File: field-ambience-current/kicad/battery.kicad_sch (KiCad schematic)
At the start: 22 parts, among them J9 JST PH 2.0 2-pin (LiPo Batter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, U7 MCP73831T-2ACI/OT (LiPo Charg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, U8 TPS61089RNR (Boost LiPo→5V, 2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

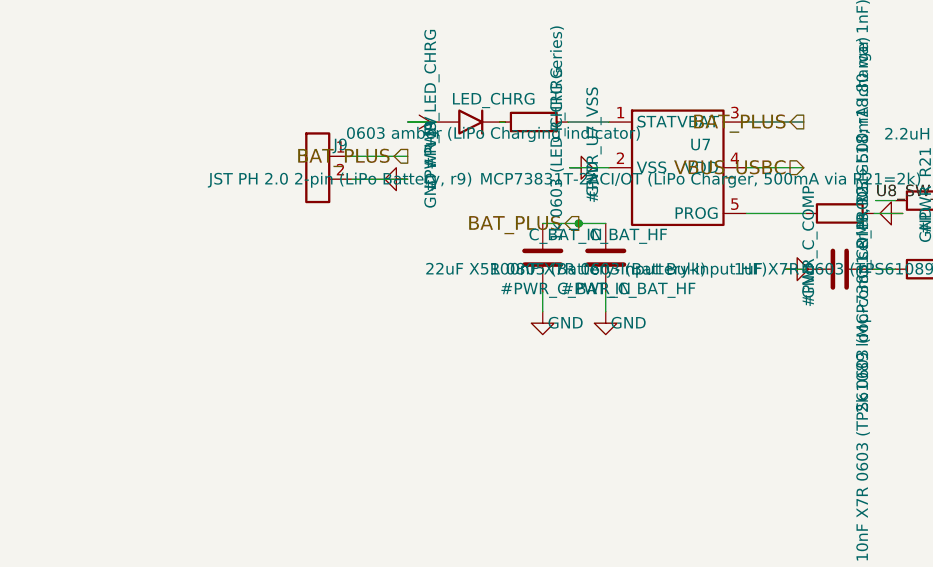
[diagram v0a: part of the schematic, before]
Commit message: fix(pcb): datasheet verification of all remaining parts — encoder + jack pad maps were dead/wrong (r18.82) (#94)
User asked to verify all other components against datasheets. Every
remaining IC and every symbol-pin<->footprint-pad pairing was checked
against the official documents (Microchip DS20001952 + DS20001984, NXP
PCA9685 Rev 4, ST USBLC6-2 + DS12110 Fig 5, Abracon via LCSC, SHOU HAN
PJ-320D, HX B3F-4055, KiCad footprint sources).

Critical pad-mapping bugs (KiCad matches pin number to pad name as a
STRING):

1. All 4 rotary encoders were completely unconnected: the official KiCad
   footprint RotaryEncoder_Alps_EC11E-Switch_Vertical_H20mm uses NAMED
   pads A/B/C/S1/S2, the custom symbol used numeric pins 1-5 - not a
   single encoder pin would have joined a pad in the netlist. Symbol pin
   numbers renamed to the pad names (footprint geometry verified from
   the KiCad GitLab source: A(0,0), C(0,2.5) = middle common, B(0,5) =
   ALPS A-C-B terminal order).

2. PJ-320D jacks (J8 line-out, J10 MIDI): pad map was wrong. The SHOU HAN
   drawing (PCB layout + schematic) assigns pad 1=A=sleeve, 2=D=ring,
   3=C=tip-switch(detect), 4=B=tip. The symbol mapped T=1/R=2/S=3/DET=4,
   which put LEFT AUDIO on the grounded sleeve barrel, GND on the detect
   contact and JACK_DETECT on the tip. Corrected to T=4/R=2/S=1/DET=3.
   Vendored footprint geometry matches the drawing exactly (3.0/4.0mm
   pad pitch, 1.0mm locators at 7.0mm) - closes TODO B0b.

3. Consequence of the true detect topology (detect rests on the TIP when
   unplugged, i.e. on the DAC L output at +-3Vpk): added R_DET_J8 10k
   (limits MCP input-clamp current to <300uA - unprotected it would have
   clamped negative half-waves through 22R at >100mA, distorting the
   speaker feed) and C_DET_J8 1uF (filters audio AC off GPA6, fc ~16Hz).
   Levels: unplugged ~0.3V LOW, plugged 3.3V HIGH.

Datasheet-required gaps:

4. MCP73831 was missing the 4.7uF VDD input capacitor from the DS typical
   application - the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
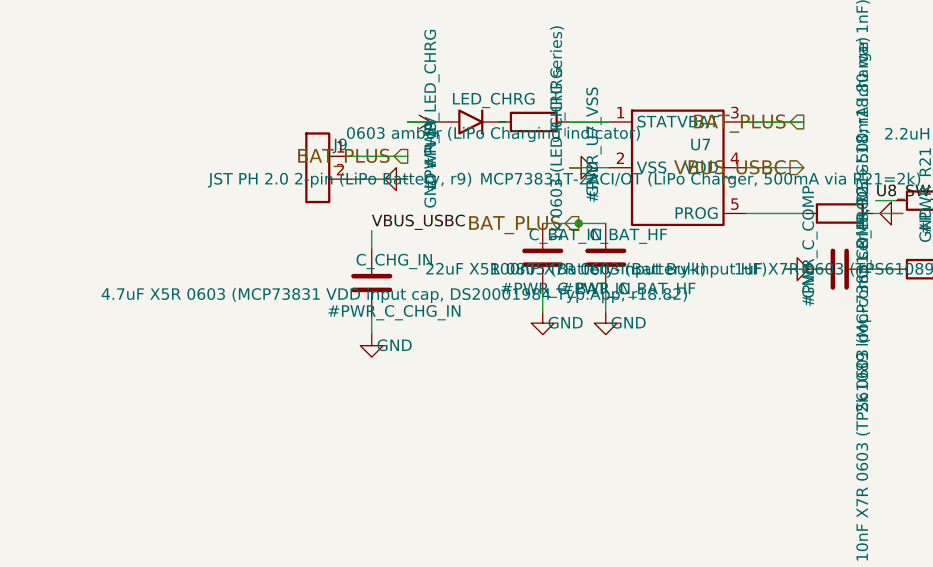
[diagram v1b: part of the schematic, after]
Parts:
- added C_CHG_IN: 4.7uF X5R 0603 (MCP73831 VDD input cap, DS2000198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, Capacitor_SMD:C_0603_1608Metric, symbol Device:C
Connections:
- net GND: now also C_CHG_IN.2
- net VBUS_USBC: now also C_CHG_IN.1
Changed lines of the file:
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@@
       (project "field_ambience"
         (path "/f6a664dc-7032-4108-a10b-e4076008e6bd" (reference "#PWR_LED_CHRG") (unit 1)))))
+  (symbol (lib_id "Device:C") (at 56 92.81 0) (unit 1)
+    (in_bom yes) (on_board yes) (dnp no)
+      (property "Reference" "C_CHG_IN" (at 58.54 90.27 0)
+        (effects (font (size 1.27 1.27))))
+      (property "Value" "4.7uF X5R 0603 (MCP73831 VDD input cap, DS20001984 Typ.App; r18.82)" (at 58.54 94.08 0)
+        (effects (font (size 1.27 1.27))))
+      (property "Footprint" "Capacitor_SMD:C_0603_1608Metric" (at 56 92.81 0)
+        (effects (font (size 1.27 1.27)) hide))
+      (property "Datasheet" "~" (at 56 92.81 0)
+        (effects (font (size 1.27 1.27)) hide))
+      (property "MPN" "GRM188R61A475KE15D" (at 58.54 96.62 0)
+        (effects (font (size 1.27 1.27)) hide))
+      (property "LCSC" "C46653" (at 58.54 97.89 0)
+        (effects (font (size 1.27 1.27)) hide))
+    (instances
+      (project "field_ambience"
+        (path "/f6a664dc-7032-4108-a10b-e4076008e6bd" (reference "C_CHG_IN") (unit 1)))))
+  (symbol (lib_id "Power:GND") (at 56 98.5 0) (unit 1)
+    (in_bom yes) (on_board yes) (dnp no)
+      (property "Reference" "#PWR_C_CHG_IN" (at 58.54 95.96 0)
+        (effects (font (size 1.27 1.27))))
+      (property "Value" "GND" (at 58.54 99.77 0)
+        (effects (font (size 1.27 1.27))))
+      (property "Footprint" "" (at 56 98.5 0)
+        (effects (font (size 1.27 1.27)) hide))
+      (property "Datasheet" "~" (at 56 98.5 0)
+        (effects (font (size 1.27 1.27)) hide))
+    (instances
+      (project "field_ambience"
+        (path "/f6a664dc-7032-4108-a10b-e4076008e6bd" (reference "#PWR_C_CHG_IN") (unit 1)))))
   (symbol (lib_id "Device:R") (at 108.0 85.08 90) (unit 1)
     (in_bom yes) (on_board yes) (dnp no)
@@
     (stroke (width 0) (type default))
 )
+  (wire (pts (xy 56 87) (xy 56 89))
+    (stroke (width 0) (type default))
+)
+  (wire (pts (xy 56 96.62) (xy 56 98.5))
+    (stroke (width 0) (type default))
+)
   (wire (pts (xy 97.62 74.92) (xy 104.0 74.92))
     (stroke (width 0) (type default))
@@
   (junction (at 140 83.65) (diameter 0) (color 0 0 0 0)
 )
+  (label "VBUS_USBC" (at 56 87 0) (fields_autoplaced)
+    (effects (font (size 1.27 1.27)) (justify left bottom))
+)
   (label "U8_SW_NODE" (at 141 83.65 0) (fields_autoplaced)

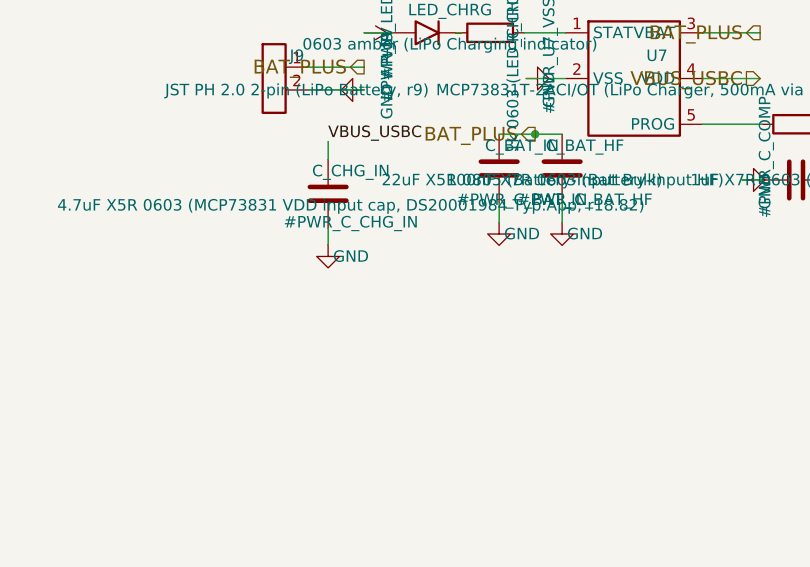
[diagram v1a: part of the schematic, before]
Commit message: fix(pcb): both PCA9685 /OE pull-ups had no driver — LEDs would never light; +mounting holes +test points +cost estimate (r18.84)
User asked whether any must-have components are missing, and for a fresh
JLC cost estimate.

CRITICAL find: both PCA9685 output-enable pins (R_OE on U6, R_OE2 on U10)
were pulled HIGH to +3V3 with a comment claiming firmware drives /OE low
after PWM init — but no net connected /OE to any MCU/MCP pin, so nothing
could ever drive it. /OE would sit HIGH forever: all 15 status LEDs, the
LCD backlight AND the 8 VU LEDs permanently disabled (backlight off = the
screen is unreadable). Fixed to pull-DOWN (outputs always enabled).
Boot-dark is still guaranteed by the chip itself: NXP datasheet Table 7,
LEDn_OFF_H[4] 'full OFF' defaults to 1 on every channel, verified against
the PDF — the part powers up with every channel in FULL_OFF regardless of
/OE. Firmware pca_init comments updated to match (nothing to sequence).

Added missing must-haves:
- 4x M2.5 mounting holes H1-H4 (plated, GND) — defined in the mechanical
  spec section 6 all along ((12,6)/(240,6)/(12,96)/(240,96)) but never in
  the schematic. DNP symbols with footprint MountingHole_2.7mm_M2.5_Pad
  (FP note: KiCad's 5.4mm pad vs the spec's 6mm — a layout call for Aron).
- 7 test points (AI_READY schematic standard requires TP_*): TP_5V,
  TP_3V3, TP_5VSW, TP_VBUS, TP_GND1/2 on power_tree + TP_BAT on battery,
  all DNP TestPoint_Pad_D1.5mm.
Both are fit-free, so jlc_bom.csv is unchanged at 58 parts / 210
placements (the exporter correctly skips the 11 DNP items).

Completeness sweep otherwise clean: USB protection (fuse+TVS+ESD+CC),
charge/power path incl. on/off (since r18.81), NRST/BOOT0, VCAP, HSE +
loads, I2C pull-ups, status LED, backlight driver, SWD, jack clamp
(r18.82). Deliberately NOT on the PCB (not defects): battery protection
PCM (must live in the LiPo pouch — buy note added), fiducials (JLC adds
them at panelization), MIDI-IN (OUT only per ADR-0004).

Cost estimate rebuilt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
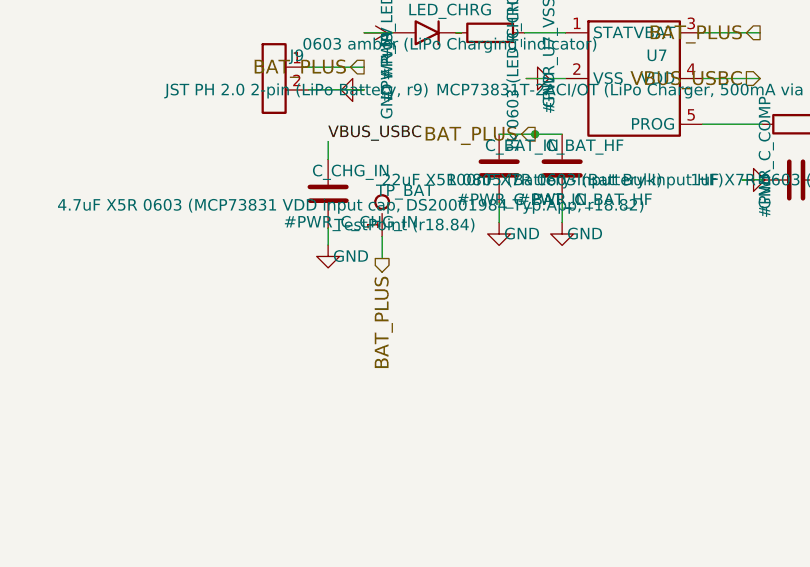
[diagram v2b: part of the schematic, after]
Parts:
- added TP_BAT: TestPoint (r18.84), TestPoint:TestPoint_Pad_D1.5mm, symbol Connector:TestPoint
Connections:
- net BAT_PLUS: now also TP_BAT.1
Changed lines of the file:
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@@
       (project "field_ambience"
         (path "/f6a664dc-7032-4108-a10b-e4076008e6bd" (reference "#PWR_C_BAT_IN") (unit 1)))))
+  (symbol (lib_id "Connector:TestPoint") (at 62 95 0) (unit 1)
+    (in_bom yes) (on_board yes) (dnp no)
+      (property "Reference" "TP_BAT" (at 64.54 92.46 0)
+        (effects (font (size 1.27 1.27))))
+      (property "Value" "TestPoint (r18.84)" (at 64.54 96.27 0)
+        (effects (font (size 1.27 1.27))))
+      (property "Footprint" "TestPoint:TestPoint_Pad_D1.5mm" (at 62 95 0)
+        (effects (font (size 1.27 1.27)) hide))
+      (property "Datasheet" "~" (at 62 95 0)
+        (effects (font (size 1.27 1.27)) hide))
+      (property "DNP" "true (Testpad, nichts zu bestuecken)" (at 64.54 98.81 0)
+        (effects (font (size 1.27 1.27)) hide))
+    (instances
+      (project "field_ambience"
+        (path "/f6a664dc-7032-4108-a10b-e4076008e6bd" (reference "TP_BAT") (unit 1)))))
   (symbol (lib_id "Device:C") (at 82 90 0) (unit 1)
     (in_bom yes) (on_board yes) (dnp no)
@@
     (stroke (width 0) (type default))
 )
+  (wire (pts (xy 62 97.54) (xy 62 100))
+    (stroke (width 0) (type default))
+)
   (wire (pts (xy 82 86.19) (xy 79 86.19))
     (stroke (width 0) (type default))
@@
     (effects (font (size 1.524 1.524)) (justify right))
 )
+  (hierarchical_label "BAT_PLUS" (shape output) (at 62 100 90)
+    (effects (font (size 1.524 1.524)) (justify right))
+)
